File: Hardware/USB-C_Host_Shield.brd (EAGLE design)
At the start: 53.3 x 59.7 mm, 109 parts, among them J1 USB-C, J2 GPIN, J3 GPOUT, U1 ARDUINO_UNO_R3_SHIELDNOLABELS, U2 LM1117, U3 74HC4050, U5 MAX3421, U6 3.3V/150mA, Y1 12.0mhZ

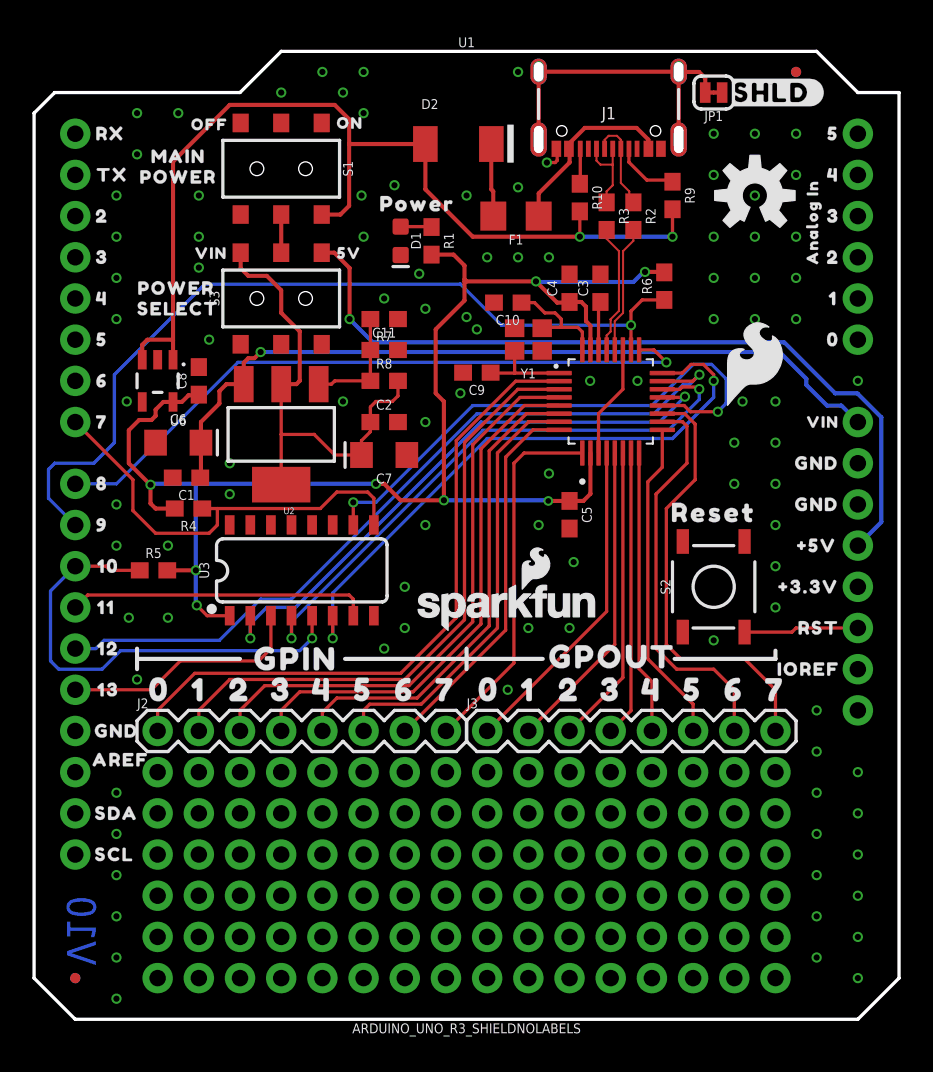
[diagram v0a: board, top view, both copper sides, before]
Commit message: Completed updates and created production files
Completed all the items in the list of items to change in testing design document, along with adding the production files and gerbers/CAM for ordering PCBs
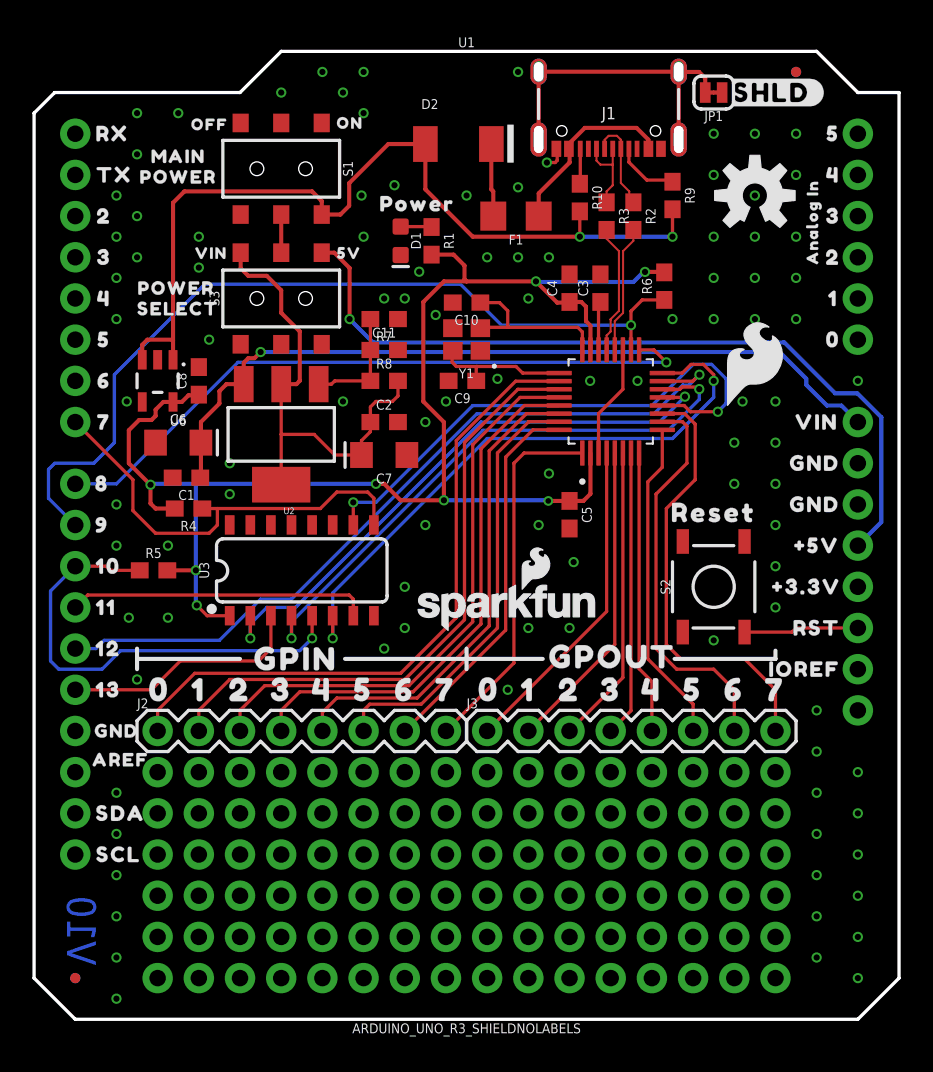
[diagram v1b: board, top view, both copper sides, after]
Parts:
- removed U$61: (no value), output:VIN7
- removed U$63: (no value), output:IOREF131211211109876543235
- added U$64: (no value), output:RX13
- added U$65: (no value), output:TX1131211211109876543245
- U$33: device output:#3#3V131211211109876543234 -> output:#5V4
- U$34: device output:#5V131211211109876543234 -> output:VIN6
- U$35: device output:GND131211211109876543229 -> output:GND131211109817654321131211211109876543260
- U$36: device output:GND131211211109876543229 -> output:SDA131211109817654321131211211109876543261
- U$38: device output:RX14 -> output:21131211211109876543246
- U$39: device output:TX15 -> output:321131211211109876543247
- U$40, U$57: device output:216 -> output:4321131211211109876543248
- U$41, U$58: device output:3217 -> output:54321131211211109876543249
- U$42: device output:43218 -> output:654321131211211109876543250
- U$43: device output:543219 -> output:7654321131211211109876543251
- U$44: device output:6543220 -> output:17654321131211211109876543252
- U$45: device output:76543221 -> output:017654321131211211109876543253
- U$46: device output:876543222 -> output:9817654321131211211109876543255
- U$47: device output:9876543223 -> output:109817654321131211211109876543256
- U$48: device output:109876543224 -> output:11109817654321131211211109876543257
- U$49: device output:11109876543225 -> output:1211109817654321131211211109876543258
- U$50: device output:1211211109876543227 -> output:131211109817654321131211211109876543259
- U$51: device output:131211211109876543228 -> output:GND131211109817654321131211211109876543260
- U$53: device output:SDA131211211109876543231 -> output:SCL131211109817654321131211211109876543262
- U$54: device output:SCL131211211109876543232 -> output:IOREF131211109817654321131211211109876543264
- U$55: device output:0131211211109876543236 -> output:21131211211109876543246
- U$56: device output:1131211211109876543239 -> output:321131211211109876543247
- U$59: device output:43218 -> output:817654321131211211109876543254
- U$60: device output:543219 -> output:RST131211109817654321131211211109876543265
- U$62: device output:RST131211211109876543234 -> output:#3#3V4
- moved U$59 48.9 mm to (4.19, 30.5)
- moved U$36 48.0 mm to (5.33, 10.2)
- moved U$51 45.7 mm to (48.1, 31.8)
- moved U$44 45.4 mm to (49.3, 41.9)
- moved U$45 45.4 mm to (49.3, 39.4)
- moved U$54 44.1 mm to (47.5, 19.1)
- moved U$60 30.5 mm to (48.3, 21.6)
- moved U$34 7.62 mm to (48.3, 34.3)
- moved U$39 5.11 mm to (4.32, 44.5)
- moved U$38 5.09 mm to (4.32, 47.0)
- moved U$40 5.08 mm to (4.32, 41.9)
- moved U$41 5.08 mm to (4.32, 39.4)
- moved U$42 5.08 mm to (4.32, 36.8)
- moved U$43 5.08 mm to (4.32, 34.3)
- moved U$55 5.08 mm to (49.3, 44.5)
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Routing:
- net VDD: track 62.3 -> 54.7 mm
- net XI: track 7.11 -> 10.5 mm
- net XO: track 5.61 -> 8.50 mm
- net 3.3V: track 91.0 -> 92.4 mm
- net GND: vias 100 -> 103

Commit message: Updates to layout as per Design review notes
Updates to notation in schematic, adjusted routing for better GND pour connections
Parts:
- added U$61: (no value), output:#_4#6
- added U$63: (no value), output:#_5#6
- added U$66: (no value), output:#_3#6
- added U$67: (no value), output:#_2#6
- added U$68: (no value), output:#_1#6
- added U$69: (no value), output:#_0#6
- added U$70: (no value), output:#_VIN#6
- added U$71, U$72: (no value), output:#_GND#7
- added U$73: (no value), output:#_#5V#8
- added U$74: (no value), output:#_#3#3V#8
- added U$75: (no value), output:#_RST#8
- added U$76: (no value), output:#_IOREF#9
- added U$77: (no value), output:#RX_#10
- added U$78: (no value), output:#TX_#11
- added U$79: (no value), output:#2_#12
- added U$80: (no value), output:#3_#12
- added U$81: (no value), output:#4_#12
- added U$82: (no value), output:#5_#12
- added U$83: (no value), output:#6_#12
- added U$84: (no value), output:#7#RESET_#12
- added U$85: (no value), output:#8#GPX_#12
- added U$86: (no value), output:#9#INT_#12
- added U$87: (no value), output:#10#CS_#12
- added U$88: (no value), output:#11#PICO_#12
- added U$89: (no value), output:#12#POCI_#12
- added U$90: (no value), output:#13#SCK_#13
- added U$92: (no value), output:#GND#21
- added U$93: (no value), output:#SDA#18
- added U$94: (no value), output:#SCL#19
- added U$95: (no value), output:#AREF#20
- moved R6 0.77 mm to (39.6, 42.5), turned to 0 degrees
- renumbered JP1 to SHLD
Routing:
- net GND: track 8.41 -> 11.4 mm, vias 103 -> 104
- net 3.3V: track 92.4 -> 95.0 mm
- net INT: track 53.0 -> 54.4 mm
- net VDD: track 54.7 -> 55.5 mm
- net GPIN5: track 27.0 -> 26.3 mm
- net GPIN7: track 22.7 -> 22.2 mm
- net GPX: track 41.5 -> 41.0 mm

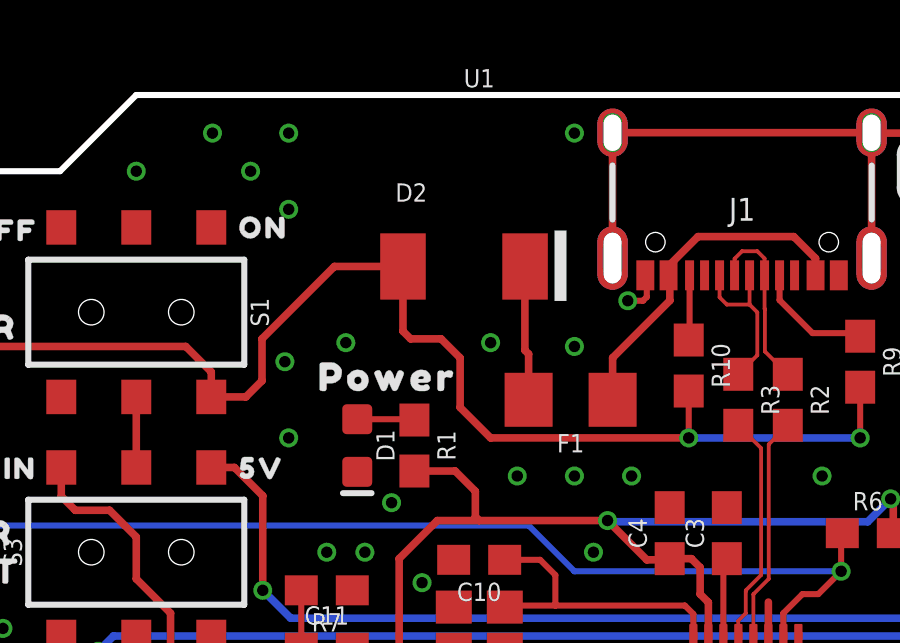
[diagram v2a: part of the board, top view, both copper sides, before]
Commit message: Updates from testing
Removed the schottky diode that was limiting the current, and replaced the fuse from the 550mA to the 750mA
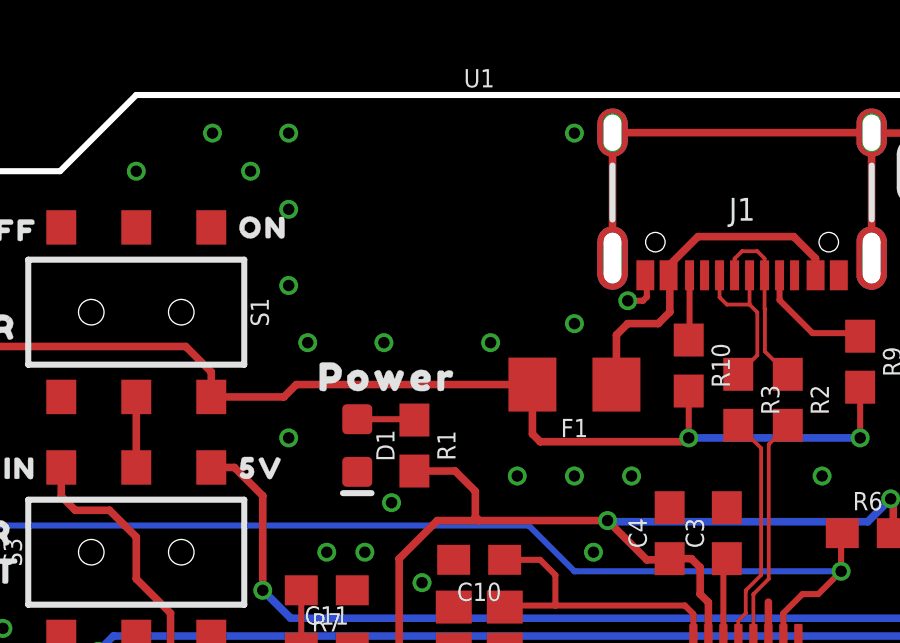
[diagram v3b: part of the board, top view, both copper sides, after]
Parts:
- removed D2: 1A/15V/220mV, SparkFun-DiscreteSemi:DO-214BA
- F1: value 6V/0.5A -> 6V/0.75A
- moved F1 0.52 mm to (29.8, 47.5)
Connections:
- removed net N$5: D2.C, F1.2
- net VDD: now also F1.2; no longer D2.A
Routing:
- net VDD: track 55.5 -> 50.3 mm
- net N$5: track 4.50 -> 0.00 mm
- net GND: vias 104 -> 105
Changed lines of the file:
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@@
 <drawing>
 <settings>
-<setting alwaysvectorfont="yes"/>
+<setting alwaysvectorfont="no"/>
 <setting verticaltext="up"/>
 </settings>
@@
 <layer number="44" name="Drills" color="7" fill="1" visible="no" active="yes"/>
 <layer number="45" name="Holes" color="7" fill="1" visible="yes" active="yes"/>
-<layer number="46" name="Milling" color="3" fill="1" visible="yes" active="yes"/>
+<layer number="46" name="Milling" color="3" fill="1" visible="no" active="yes"/>
 <layer number="47" name="Measures" color="7" fill="1" visible="no" active="yes"/>
 <layer number="48" name="Document" color="7" fill="1" visible="no" active="yes"/>
@@
 <attribute name="VALUE" x="21.971" y="45.466" size="0.6096" layer="27" font="vector" ratio="20" rot="R270" align="top-center"/>
 </element>
-<element name="F1" library="SparkFun-Fuses" package="1206" value="6V/0.5A" x="29.718" y="46.99" smashed="yes" rot="R180">
-<attribute name="NAME" x="29.718" y="45.847" size="0.6096" layer="25" font="vector" ratio="20" rot="R180" align="bottom-center"/>
-<attribute name="PROD_ID" value="RES-08585" x="14.478" y="144.78" size="1.778" layer="27" rot="R180" display="off"/>
-<attribute name="VALUE" x="29.718" y="48.133" size="0.6096" layer="27" font="vector" ratio="20" rot="R180" align="top-center"/>
-</element>
 <element name="FD1" library="SparkFun-Aesthetics" package="FIDUCIAL-MICRO" value="FIDUCIALUFIDUCIAL" x="2.54" y="0" smashed="yes" rot="MR0"/>
 <element name="FD2" library="SparkFun-Aesthetics" package="FIDUCIAL-MICRO" value="FIDUCIALUFIDUCIAL" x="2.54" y="0" smashed="yes" rot="R90"/>
@@
 <attribute name="SF_ID" value="COM-00597" x="15.24" y="49.911" size="1.778" layer="27" font="vector" ratio="15" rot="R180" display="off"/>
 <attribute name="VALUE" x="11.43" y="49.911" size="0.6096" layer="27" font="vector" ratio="20" rot="R270" align="top-center"/>
-</element>
-<element name="D2" library="SparkFun-DiscreteSemi" package="DO-214BA" value="1A/15V/220mV" x="26.162" y="51.435" smashed="yes">
-<attribute name="NAME" x="23.876" y="53.594" size="0.6096" layer="25" ratio="20"/>
-<attribute name="PROD_ID" value="DIO-15217" x="26.162" y="51.435" size="1.778" layer="27" font="vector" ratio="15" display="off"/>
-<attribute name="VALUE" x="23.749" y="48.641" size="0.6096" layer="27" ratio="20"/>
 </element>
 <element name="U$15" library="output" package="MAIN40" value="" x="8.89" y="50.673" smashed="yes"/>
@@
 <element name="U$95" library="output" package="#AREF#20" value="" x="4.953" y="12.7" smashed="yes" rot="MR0"/>
 <element name="U$92" library="output" package="#GND#21" value="" x="4.699" y="15.24" smashed="yes" rot="MR0"/>
+<element name="F1" library="SparkFun-Fuses" package="1206" value="6V/0.75A" x="29.845" y="47.498" smashed="yes" rot="R180">
+<attribute name="NAME" x="29.845" y="46.355" size="0.6096" layer="25" font="vector" ratio="20" rot="R180" align="bottom-center"/>
+<attribute name="PROD_ID" value="RES-11150" x="29.845" y="47.498" size="1.778" layer="27" font="vector" ratio="15" rot="R180" display="off"/>
+<attribute name="VALUE" x="29.845" y="48.641" size="0.6096" layer="27" font="vector" ratio="20" rot="R180" align="top-center"/>
+</element>
 </elements>
 <signals>
@@
 <via x="12.065" y="29.845" extent="1-16" drill="0.381"/>
 <via x="5.08" y="29.21" extent="1-16" drill="0.381"/>
-<via x="22.225" y="48.895" extent="1-16" drill="0.381"/>
+<via x="23.495" y="48.895" extent="1-16" drill="0.381"/>
 <via x="27.051" y="48.895" extent="1-16" drill="0.381"/>
 <via x="27.94" y="44.45" extent="1-16" drill="0.381"/>
@@
 <via x="5.08" y="45.72" extent="1-16" drill="0.381"/>
 <via x="10.16" y="45.72" extent="1-16" drill="0.381"/>
-<via x="20.193" y="48.26" extent="1-16" drill="0.381"/>
+<via x="20.955" y="48.895" extent="1-16" drill="0.381"/>
 <via x="20.32" y="45.72" extent="1-16" drill="0.381"/>
 <via x="23.749" y="43.561" extent="1-16" drill="0.381"/>
@@
 <via x="8.255" y="26.67" extent="1-16" drill="0.381"/>
 <via x="29.845" y="55.88" extent="1-16" drill="0.381"/>
-<via x="29.845" y="48.768" extent="1-16" drill="0.381"/>
+<via x="29.845" y="49.53" extent="1-16" drill="0.381"/>
 <via x="20.32" y="53.34" extent="1-16" drill="0.381"/>
 <via x="43.688" y="35.56" extent="1-16" drill="0.381"/>
@@
 <via x="5.08" y="16.51" extent="1-16" drill="0.381"/>
 <via x="38.1" y="44.45" extent="1-16" drill="0.381"/>
+<via x="20.32" y="50.8" extent="1-16" drill="0.381"/>
 </signal>
 <signal name="N$7">
@@
 <contactref element="J1" pad="VBUS1"/>
 <contactref element="J1" pad="VBUS2"/>
-<contactref element="F1" pad="1"/>
 <wire x1="32.983" y1="51.14" x2="33.0253625" y2="51.0976375" width="0.254" layer="1"/>
-<wire x1="33.0253625" y1="51.0976375" x2="33.0253625" y2="50.2973625" width="0.254" layer="1"/>
-<wire x1="31.118" y1="48.39" x2="33.0253625" y2="50.2973625" width="0.254" layer="1"/>
 <wire x1="32.983" y1="51.14" x2="32.983" y2="51.4492125" width="0.254" layer="1"/>
 <wire x1="37.883" y1="51.703215625" x2="37.883" y2="51.14" width="0.254" layer="1"/>
@@
 <wire x1="32.983" y1="51.4492125" x2="33.9637875" y2="52.43" width="0.254" layer="1"/>
 <wire x1="33.9637875" y1="52.43" x2="37.1562125" y2="52.43" width="0.254" layer="1"/>
-<wire x1="31.118" y1="48.39" x2="31.118" y2="46.99" width="0.254" layer="1"/>
+<wire x1="33.0253625" y1="49.9163625" x2="33.0253625" y2="51.0976375" width="0.254" layer="1"/>
+<wire x1="31.245" y1="49.152" x2="31.623" y2="49.53" width="0.254" layer="1"/>
+<wire x1="31.623" y1="49.53" x2="32.639" y2="49.53" width="0.254" layer="1"/>
+<wire x1="32.639" y1="49.53" x2="33.0253625" y2="49.9163625" width="0.254" layer="1"/>
+<contactref element="F1" pad="1"/>
+<wire x1="31.245" y1="47.498" x2="31.245" y2="49.152" width="0.254" layer="1"/>
 </signal>
 <signal name="5V">
@@
 </signal>
 <signal name="VDD">
-<contactref element="D2" pad="A"/>
 <via x="33.655" y="45.72" extent="1-16" drill="0.381"/>
-<wire x1="27.051" y1="45.72" x2="33.655" y2="45.72" width="0.254" layer="1"/>
 <via x="39.37" y="45.72" extent="1-16" drill="0.381"/>
 <wire x1="33.655" y1="45.72" x2="39.37" y2="45.72" width="0.254" layer="16"/>
@@
 <wire x1="9.525" y1="48.768" x2="16.891" y2="48.768" width="0.254" layer="1"/>
 <wire x1="16.891" y1="48.768" x2="17.74" y2="47.919" width="0.254" layer="1"/>
-<wire x1="17.74" y1="47.086" x2="18.892" y2="47.086" width="0.254" layer="1"/>
-<wire x1="18.892" y1="47.086" x2="19.431" y2="47.625" width="0.254" layer="1"/>
-<wire x1="19.431" y1="47.625" x2="19.431" y2="49.022" width="0.254" layer="1"/>
-<wire x1="21.844" y1="51.435" x2="24.13" y2="51.435" width="0.254" layer="1"/>
-<wire x1="19.431" y1="49.022" x2="21.844" y2="51.435" width="0.254" layer="1"/>
-<wire x1="24.384" y1="49.022" x2="25.4" y2="49.022" width="0.254" layer="1"/>
-<wire x1="25.4" y1="49.022" x2="26.035" y2="48.387" width="0.254" layer="1"/>
-<wire x1="26.035" y1="46.736" x2="27.051" y2="45.72" width="0.254" layer="1"/>
-<wire x1="24.13" y1="51.435" x2="24.13" y2="49.276" width="0.254" layer="1"/>
-<wire x1="24.13" y1="49.276" x2="24.384" y2="49.022" width="0.254" layer="1"/>
-<wire x1="26.035" y1="48.387" x2="26.035" y2="46.736" width="0.254" layer="1"/>
-</signal>
-<signal name="N$5">
+<wire x1="20.162" y1="47.086" x2="20.574" y2="47.498" width="0.254" layer="1"/>
+<wire x1="17.74" y1="47.086" x2="20.162" y2="47.086" width="0.254" layer="1"/>
+<wire x1="28.445" y1="47.498" x2="20.574" y2="47.498" width="0.254" layer="1"/>
+<wire x1="28.445" y1="45.85" x2="28.702" y2="45.593" width="0.254" layer="1"/>
+<wire x1="28.702" y1="45.593" x2="33.528" y2="45.593" width="0.254" layer="1"/>
+<wire x1="33.528" y1="45.593" x2="33.655" y2="45.72" width="0.254" layer="1"/>
 <contactref element="F1" pad="2"/>
-<contactref element="D2" pad="C"/>
-<wire x1="28.318" y1="46.99" x2="28.318" y2="48.517" width="0.254" layer="1"/>
-<wire x1="28.318" y1="48.517" x2="28.194" y2="48.641" width="0.254" layer="1"/>
-<wire x1="28.194" y1="48.641" x2="28.194" y2="51.429" width="0.254" layer="1"/>
-<wire x1="28.194" y1="51.429" x2="28.2" y2="51.435" width="0.254" layer="1"/>
+<wire x1="28.445" y1="47.498" x2="28.445" y2="45.85" width="0.254" layer="1"/>
 </signal>
 <signal name="N$2">
